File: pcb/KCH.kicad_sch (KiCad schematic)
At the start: 15 parts, among them J1 CTBP9550/2, J2 Write EEPROM, J3 40HAT, J4 Serial, U1 CAT24C32WI

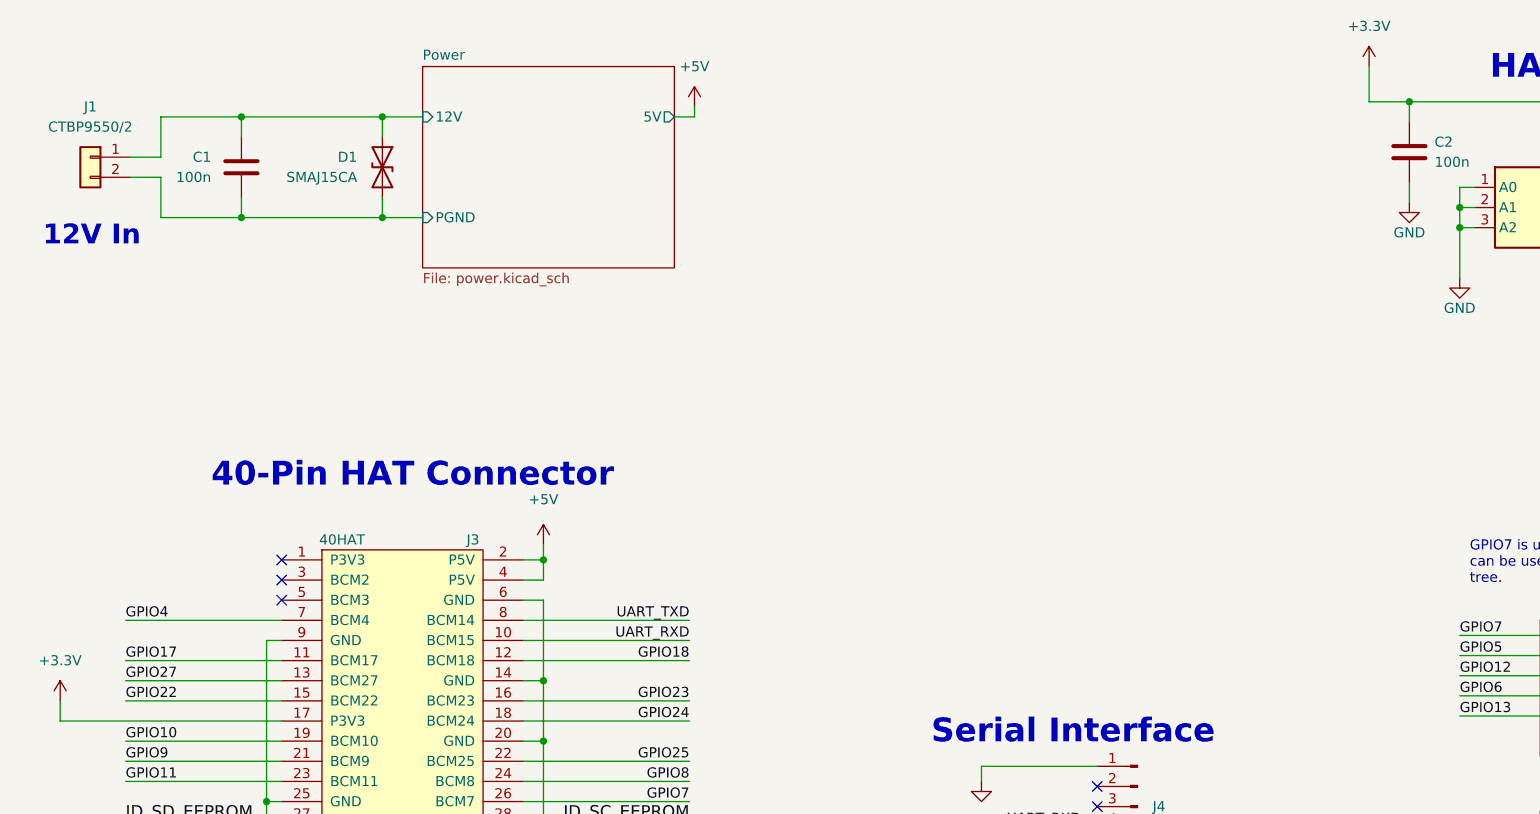
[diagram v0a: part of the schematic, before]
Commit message: Update to kicad 8
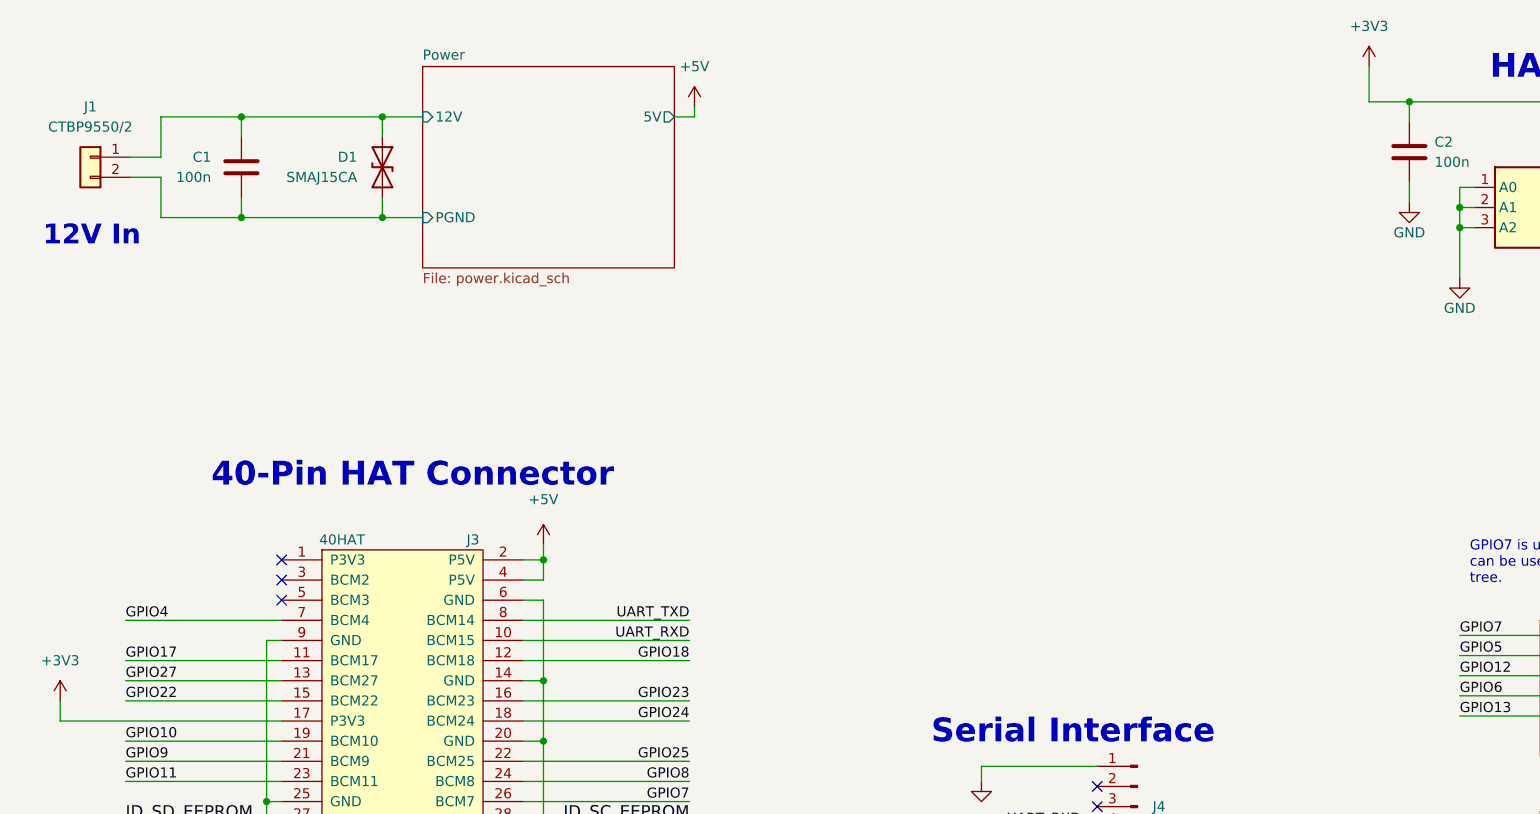
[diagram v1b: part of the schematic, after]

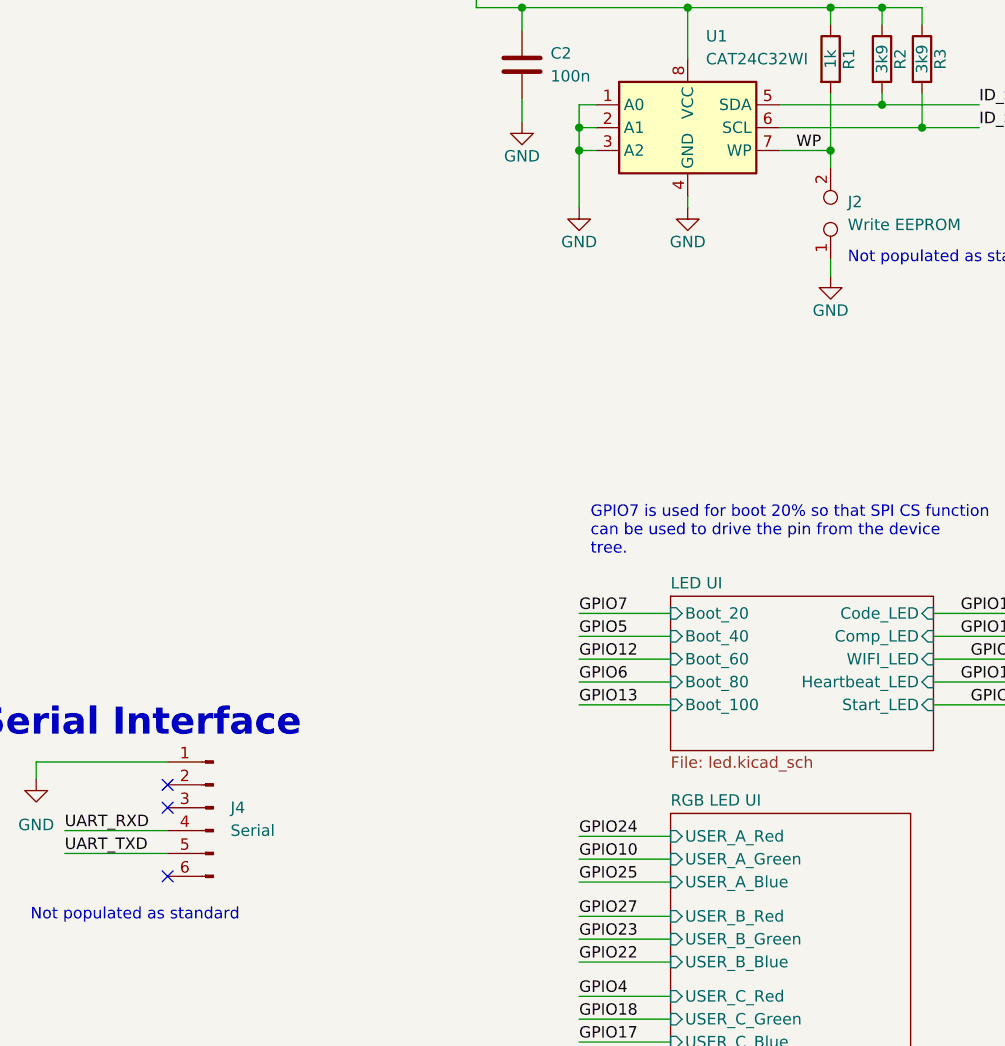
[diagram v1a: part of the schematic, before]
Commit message: Fix JLC part association
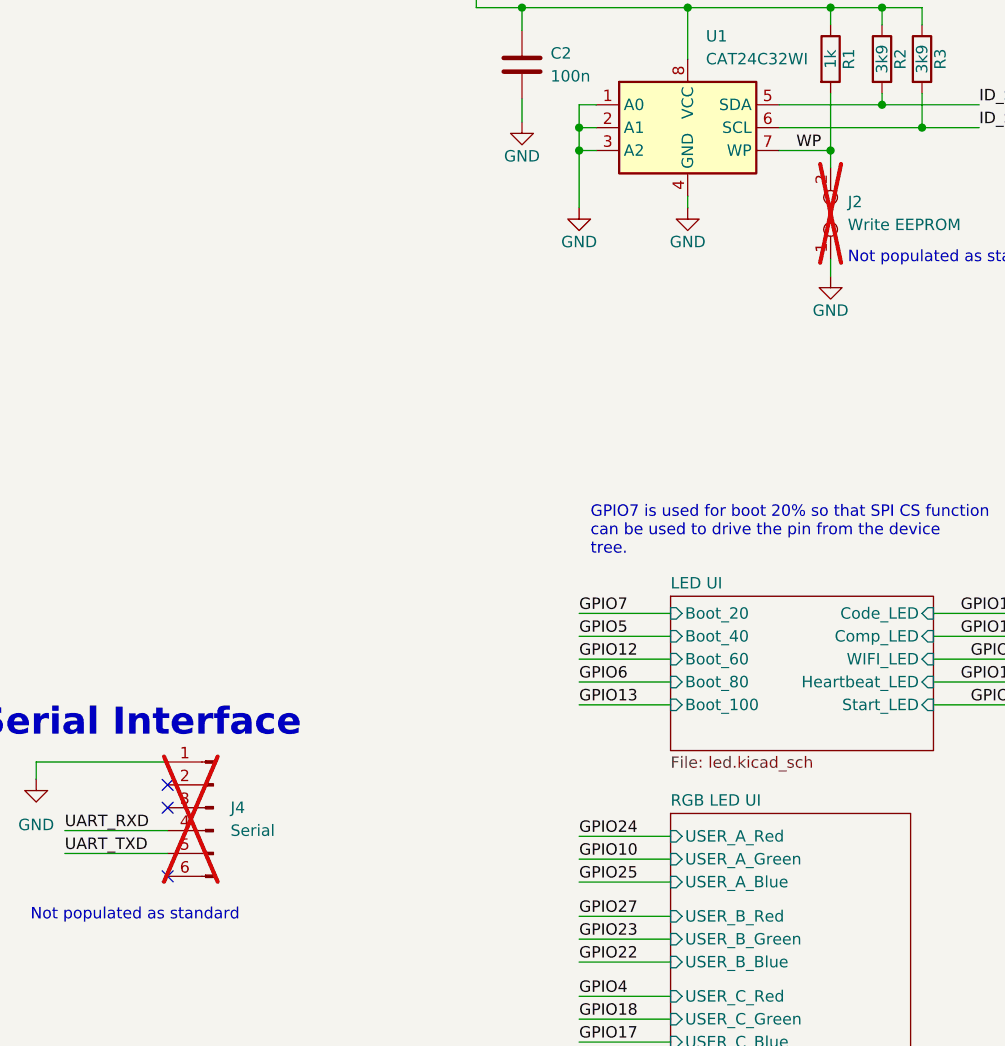
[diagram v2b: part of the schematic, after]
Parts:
- C1, C2: JLC (none) -> C307331
- D1: JLC (none) -> C110044
- J2, J4: now not fitted
- R1: JLC (none) -> C11702
- R2, R3: JLC (none) -> C51721
- U1: JLC (none) -> C81193
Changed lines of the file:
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@@
+			)
+		)
+		(property "JLC" ""
+			(at 58.42 165.1 0)
+			(effects
+				(font
+					(size 1.27 1.27)
+				)
+				(hide yes)
 			)
 		)
@@
 			)
 		)
+		(property "JLC" ""
+			(at 83.185 165.1 0)
+			(effects
+				(font
+					(size 1.27 1.27)
+				)
+				(hide yes)
+			)
+		)
 		(pin "1"
 		)
@@
 			)
 		)
+		(property "JLC" ""
+			(at 58.42 180.975 0)
+			(effects
+				(font
+					(size 1.27 1.27)
+				)
+				(hide yes)
+			)
+		)
 		(pin "1"
 		)
@@
 			)
 		)
+		(property "JLC" ""
+			(at 83.185 180.975 0)
+			(effects
+				(font
+					(size 1.27 1.27)
+				)
+				(hide yes)
+			)
+		)
 		(pin "1"
 		)
@@
 			)
 		)
+		(property "JLC" ""
+			(at 69.215 87.63 0)
+			(effects
+				(font
+					(size 1.27 1.27)
+				)
+				(hide yes)
+			)
+		)
 		(pin "1"
 		)
@@
 			)
 		)
+		(property "JLC" "C51721"
+			(at 236.22 35.56 0)
+			(effects
+				(font
+					(size 1.27 1.27)
+				)
+				(hide yes)
+			)
+		)
 		(pin "1"
 		)
@@
 		(in_bom no)
 		(on_board yes)
-		(dnp no)
+		(dnp yes)
 		(fields_autoplaced yes)
 		(property "Reference" "J2"
@@
 			)
 		)
+		(property "JLC" ""
+			(at 230.505 52.705 0)
+			(effects
+				(font
+					(size 1.27 1.27)
+				)
+				(hide yes)
+			)
+		)
 		(pin "1"
 		)
@@
 			)
 		)
+		(property "JLC" "C110044"
+			(at 66.675 38.1 0)
+			(effects
+				(font
+					(size 1.27 1.27)
+				)
+				(hide yes)
+			)
+		)
 		(pin "1"
 		)
@@
 		)
 		(property "Description" ""
+			(at 230.505 35.56 0)
+			(effects
+				(font
+					(size 1.27 1.27)
+				)
+				(hide yes)
+			)
+		)
+		(property "JLC" "C11702"
 			(at 230.505 35.56 0)
 			(effects
@@
 			)
 		)
+		(property "JLC" ""
+			(at 29.845 36.83 0)
+			(effects
+				(font
+					(size 1.27 1.27)
+				)
+				(hide yes)
+			)
+		)
 		(pin "1"
 		)
@@
 		)
 		(property "Description" ""
+			(at 240.665 35.56 0)
+			(effects
+				(font
+					(size 1.27 1.27)
+				)
+				(hide yes)
+			)
+		)
+		(property "JLC" "C51721"
 			(at 240.665 35.56 0)
 			(effects
@@
 			)
 		)
+		(property "JLC" "C81193"
+			(at 214.63 43.18 0)
+			(effects
+				(font
+					(size 1.27 1.27)
+				)
+				(hide yes)
+			)
+		)
 		(pin "1"
 		)
@@
 			)
 		)
+		(property "JLC" "C307331"
+			(at 48.895 38.1 0)
+			(effects
+				(font
+					(size 1.27 1.27)
+				)
+				(hide yes)
+			)
+		)
 		(pin "1"
 		)
@@
 		(in_bom no)
 		(on_board yes)
-		(dnp no)
+		(dnp yes)
 		(fields_autoplaced yes)
 		(property "Reference" "J4"
@@
 		)
 		(property "Description" ""
+			(at 161.925 118.745 0)
+			(effects
+				(font
+					(size 1.27 1.27)
+				)
+				(hide yes)
+			)
+		)
+		(property "JLC" ""
 			(at 161.925 118.745 0)
 			(effects
@@
 			(at 196.215 36.195 0)
 			(effects
+				(font
+					(size 1.27 1.27)
+				)
+				(hide yes)
+			)
+		)
+		(property "JLC" "C307331"
+			(at 196.215 36.195 0)
+			(effects

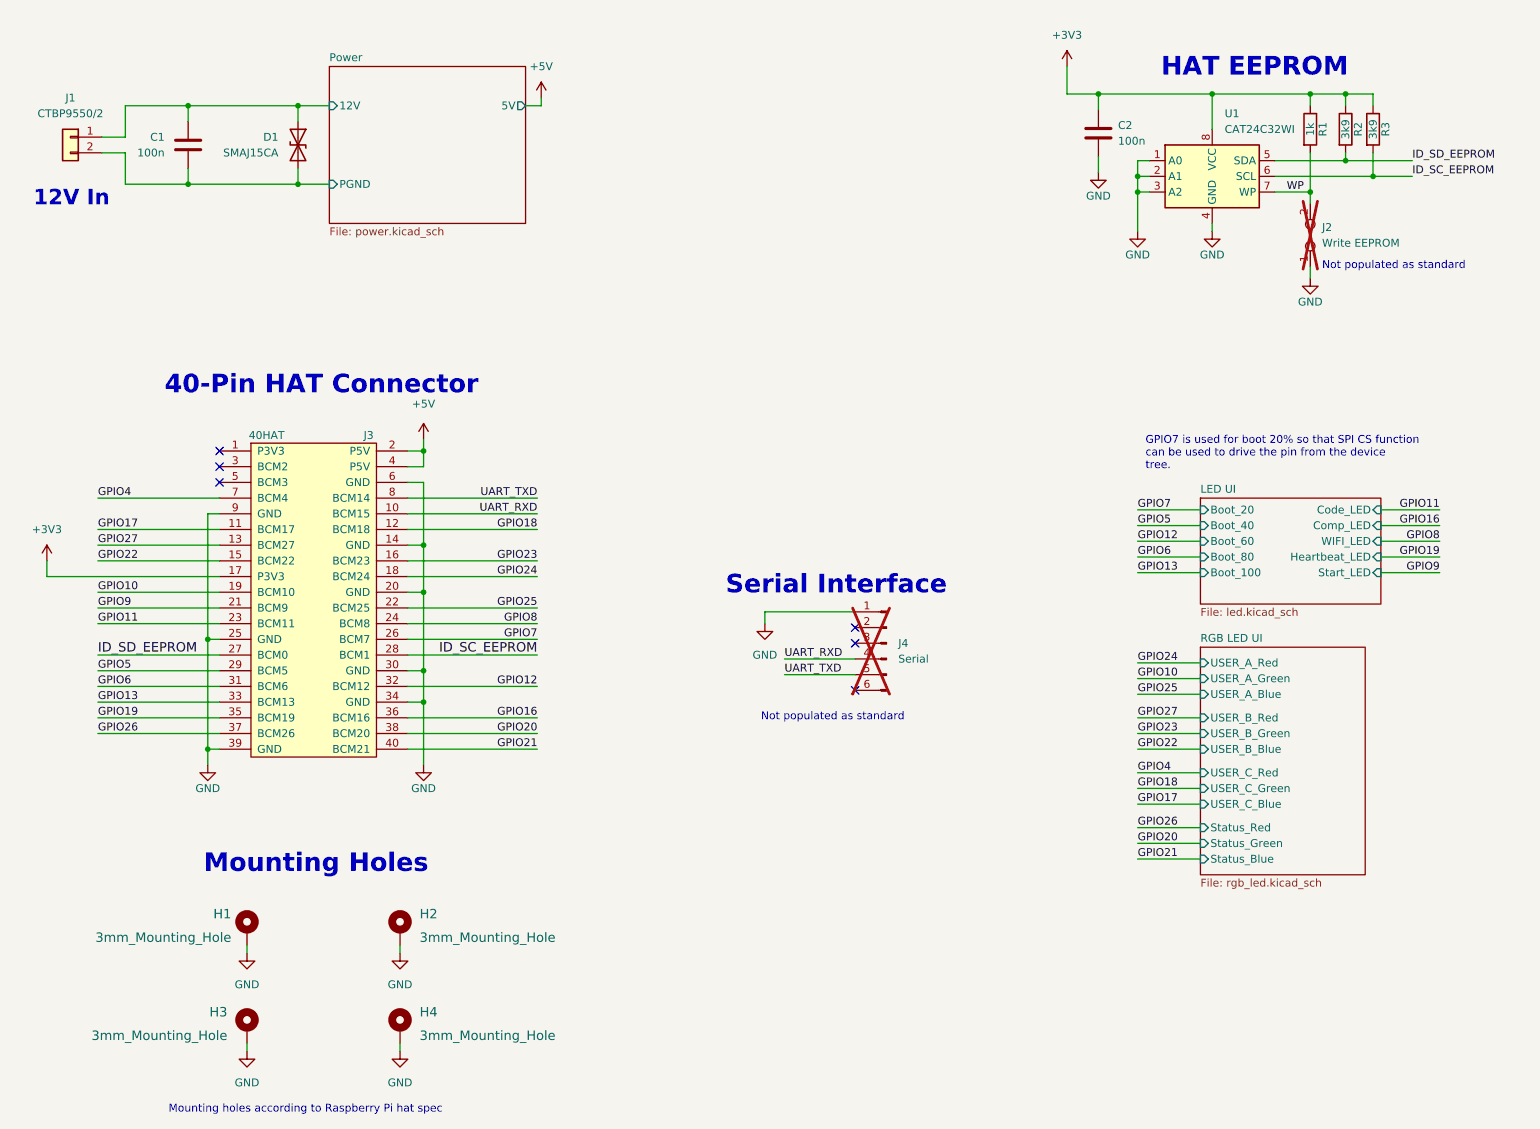
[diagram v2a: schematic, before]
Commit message: Fix ERC/DRC errors from Kicad 8
Mostly outdated library symbols and aligning the schmatic to the new grid
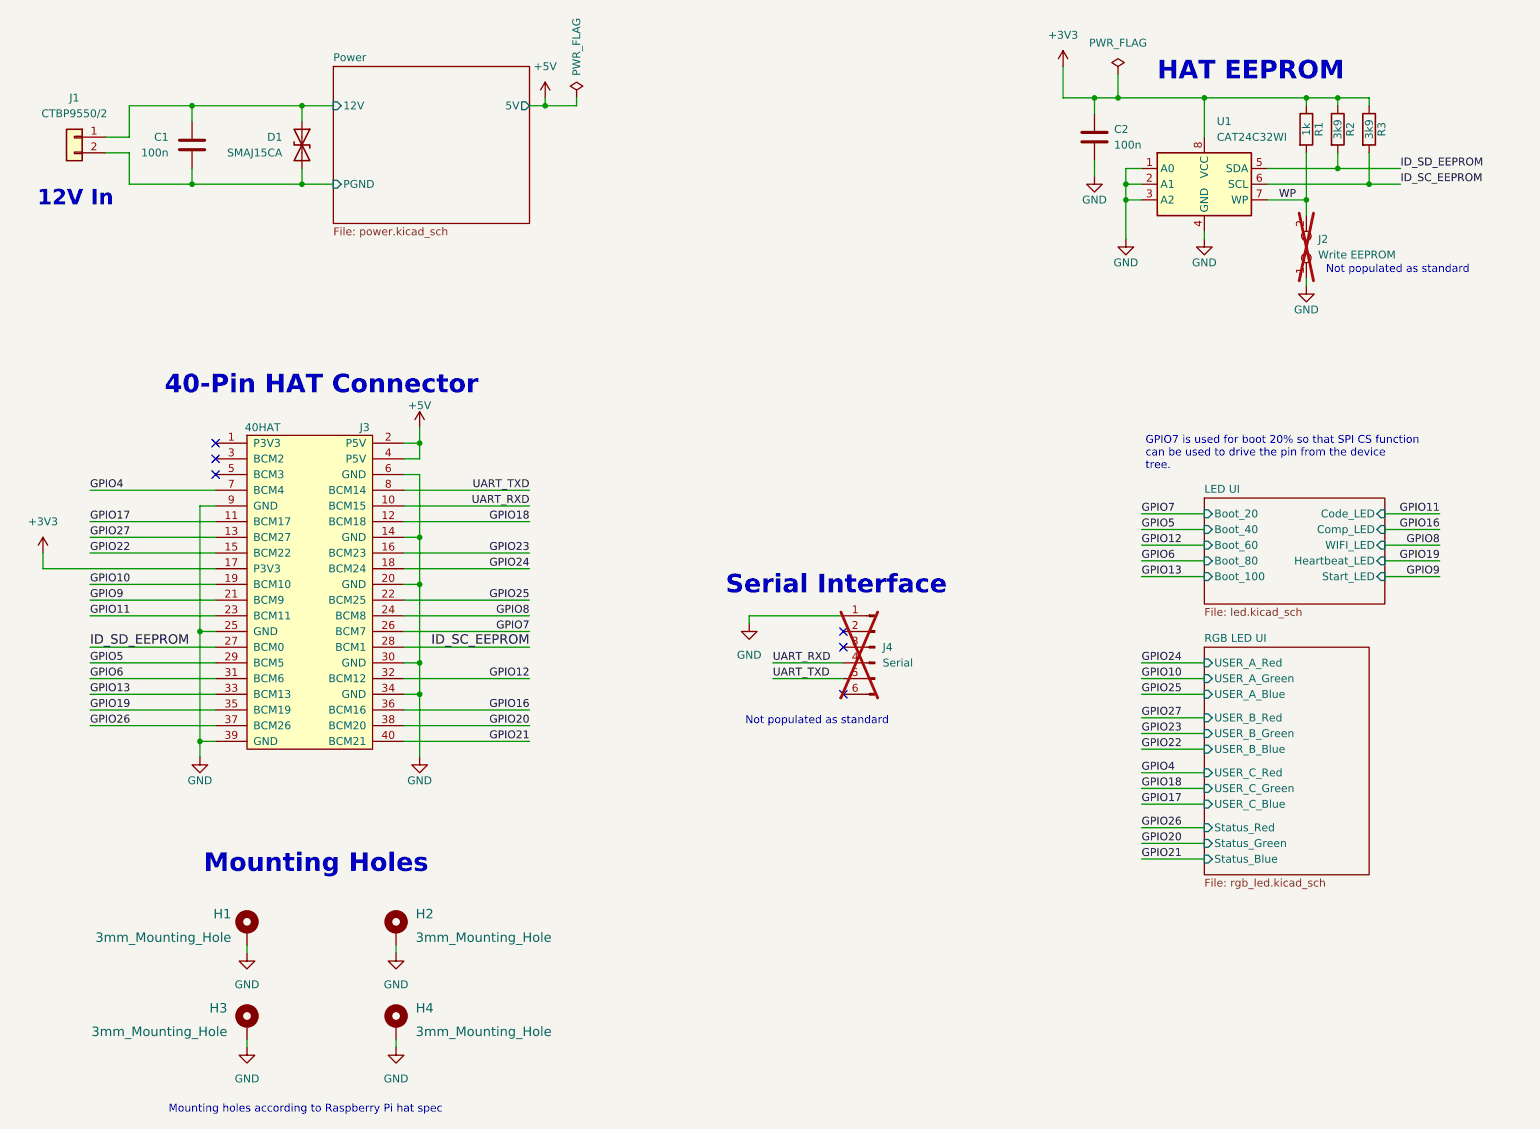
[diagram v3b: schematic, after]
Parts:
- J4: symbol Connector:Conn_01x06_Male -> Connector:Conn_01x06_Pin; now in the parts list
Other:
- moved on the sheet: C1, C2, D1, H2, H3, H4, J1, J2, J3, J4, R1, R2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
